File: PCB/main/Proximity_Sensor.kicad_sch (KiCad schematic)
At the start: 9 parts, among them U6 VL6180XV0NR_1

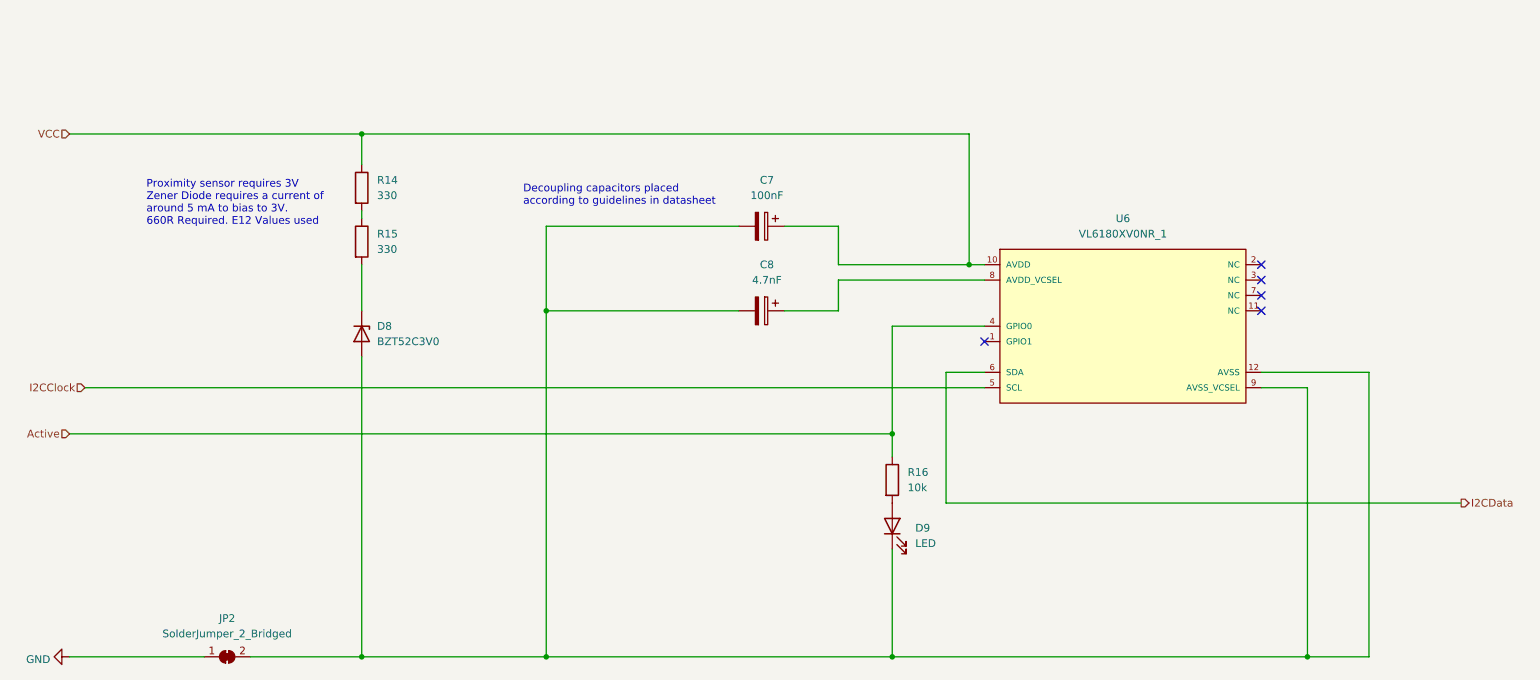
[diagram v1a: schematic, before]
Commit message: Add power flags
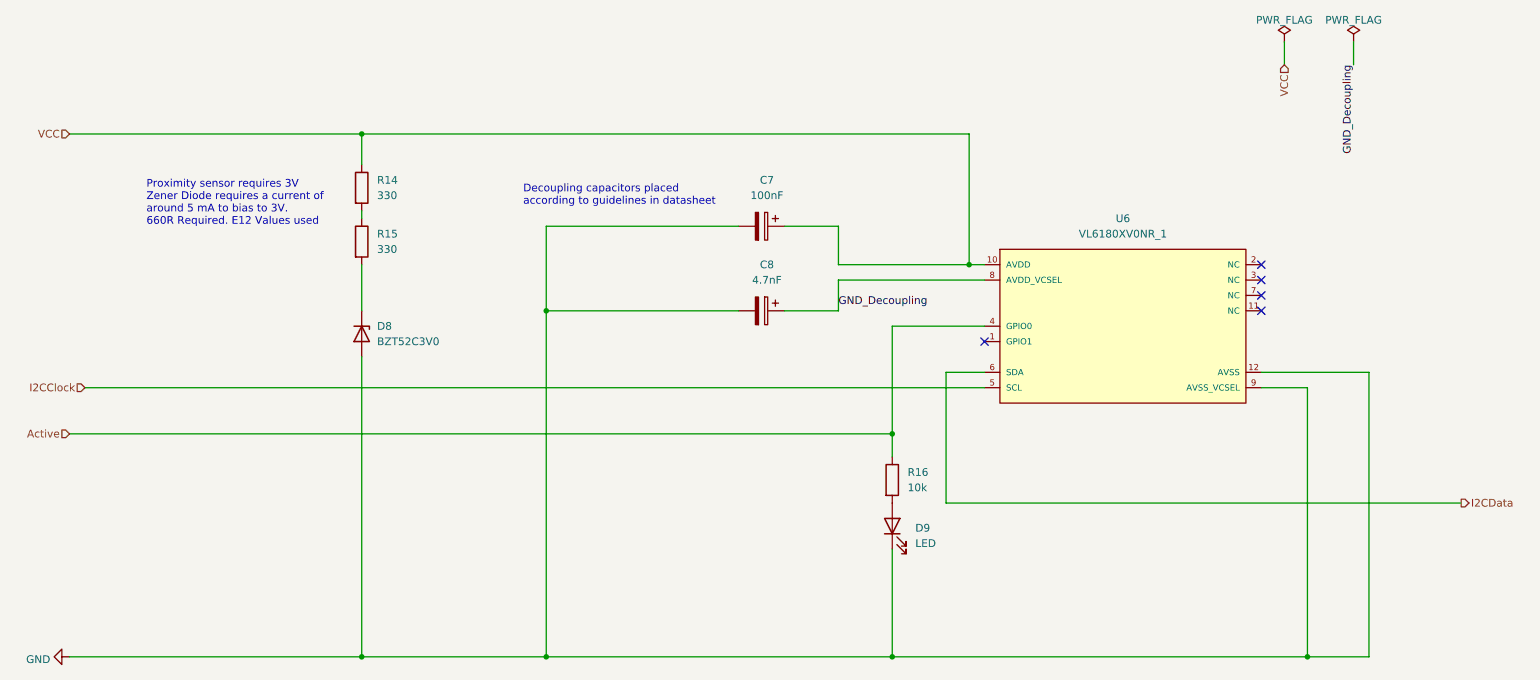
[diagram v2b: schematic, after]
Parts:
- removed JP2: SolderJumper_2_Bridged, Jumper:SolderJumper-2_P1.3mm_Bridged2Bar_Pad1.0x1.5mm, symbol Jumper:SolderJumper_2_Bridged
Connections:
- net GND: now also C7.2, C8.2, D8.2 (A), D9.1 (K), U6.12 (AVSS), U6.9 (AVSS_VCSEL)
- net GND_Decoupling: now reaches C8.1, U6.8 (AVDD_VCSEL)
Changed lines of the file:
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@@
+    (stroke (width 0) (type default) (color 0 0 0 0))
+  )
+  (wire (pts (xy 248.92 22.86) (xy 248.92 26.67))
     (stroke (width 0) (type default) (color 0 0 0 0))
   )
@@
     (stroke (width 0) (type default) (color 0 0 0 0))
   )
-  (wire (pts (xy 36.83 124.46) (xy 59.055 124.46))
-    (stroke (width 0) (type default) (color 0 0 0 0))
-  )
   (wire (pts (xy 163.83 59.69) (xy 163.83 53.34))
     (stroke (width 0) (type default) (color 0 0 0 0))
@@
     (stroke (width 0) (type default) (color 0 0 0 0))
   )
-  (wire (pts (xy 66.675 124.46) (xy 85.09 124.46))
+  (wire (pts (xy 36.83 124.46) (xy 85.09 124.46))
     (stroke (width 0) (type default) (color 0 0 0 0))
   )
@@
   )
   (wire (pts (xy 185.42 59.69) (xy 187.96 59.69))
+    (stroke (width 0) (type default) (color 0 0 0 0))
+  )
+  (wire (pts (xy 237.49 22.86) (xy 237.49 26.67))
     (stroke (width 0) (type default) (color 0 0 0 0))
   )
@@
     (effects (font (size 1.27 1.27)) (justify left bottom))
   )
+  (label "GND_Decoupling" (at 163.83 66.675 0)
+    (effects (font (size 1.27 1.27)) (justify left bottom))
+  )
+  (label "GND_Decoupling" (at 248.92 26.67 270)
+    (effects (font (size 1.27 1.27)) (justify right bottom))
+  )
   (hierarchical_label "Active" (shape input) (at 36.83 87.63 180)
     (effects (font (size 1.27 1.27)) (justify right))
   )
   (hierarchical_label "VCC" (shape input) (at 36.83 38.1 180)
+    (effects (font (size 1.27 1.27)) (justify right))
+  )
+  (hierarchical_label "VCC" (shape input) (at 237.49 26.67 270)
     (effects (font (size 1.27 1.27)) (justify right))
   )
@@
     (pin "2")
   )
-  (symbol (lib_id "Jumper:SolderJumper_2_Bridged") (at 62.865 124.46 0) (unit 1)
-    (in_bom yes) (on_board yes) (fields_autoplaced)
-    (property "Reference" "JP2" (id 0) (at 62.865 118.11 0))
-    (property "Value" "SolderJumper_2_Bridged" (id 1) (at 62.865 120.65 0))
-    (property "Footprint" "Jumper:SolderJumper-2_P1.3mm_Bridged2Bar_Pad1.0x1.5mm" (id 2) (at 62.865 124.46 0)
-      (effects (font (size 1.27 1.27)) hide)
-    )
-    (property "Datasheet" "~" (id 3) (at 62.865 124.46 0)
-      (effects (font (size 1.27 1.27)) hide)
-    )
-    (pin "1")
-    (pin "2")
+  (symbol (lib_id "power:PWR_FLAG") (at 237.49 22.86 0) (unit 1)
+    (in_bom yes) (on_board yes) (fields_autoplaced)
+    (property "Reference" "#FLG04" (id 0) (at 237.49 20.955 0)
+      (effects (font (size 1.27 1.27)) hide)
+    )
+    (property "Value" "PWR_FLAG" (id 1) (at 237.49 19.2842 0))
+    (property "Footprint" "" (id 2) (at 237.49 22.86 0)
+      (effects (font (size 1.27 1.27)) hide)
+    )
+    (property "Datasheet" "~" (id 3) (at 237.49 22.86 0)
+      (effects (font (size 1.27 1.27)) hide)
+    )
+    (pin "1")
   )
   (symbol (lib_id "power:GND") (at 36.83 124.46 270) (unit 1)
@@
     (pin "2")
   )
+  (symbol (lib_id "power:PWR_FLAG") (at 248.92 22.86 0) (unit 1)
+    (in_bom yes) (on_board yes) (fields_autoplaced)
+    (property "Reference" "#FLG05" (id 0) (at 248.92 20.955 0)
+      (effects (font (size 1.27 1.27)) hide)
+    )
+    (property "Value" "PWR_FLAG" (id 1) (at 248.92 19.2842 0))
+    (property "Footprint" "" (id 2) (at 248.92 22.86 0)
+      (effects (font (size 1.27 1.27)) hide)
+    )
+    (property "Datasheet" "~" (id 3) (at 248.92 22.86 0)
+      (effects (font (size 1.27 1.27)) hide)
+    )
+    (pin "1")
+  )
   (symbol (lib_id "EEE3088Components:VL6180XV0NR_1") (at 185.42 59.69 0) (unit 1)

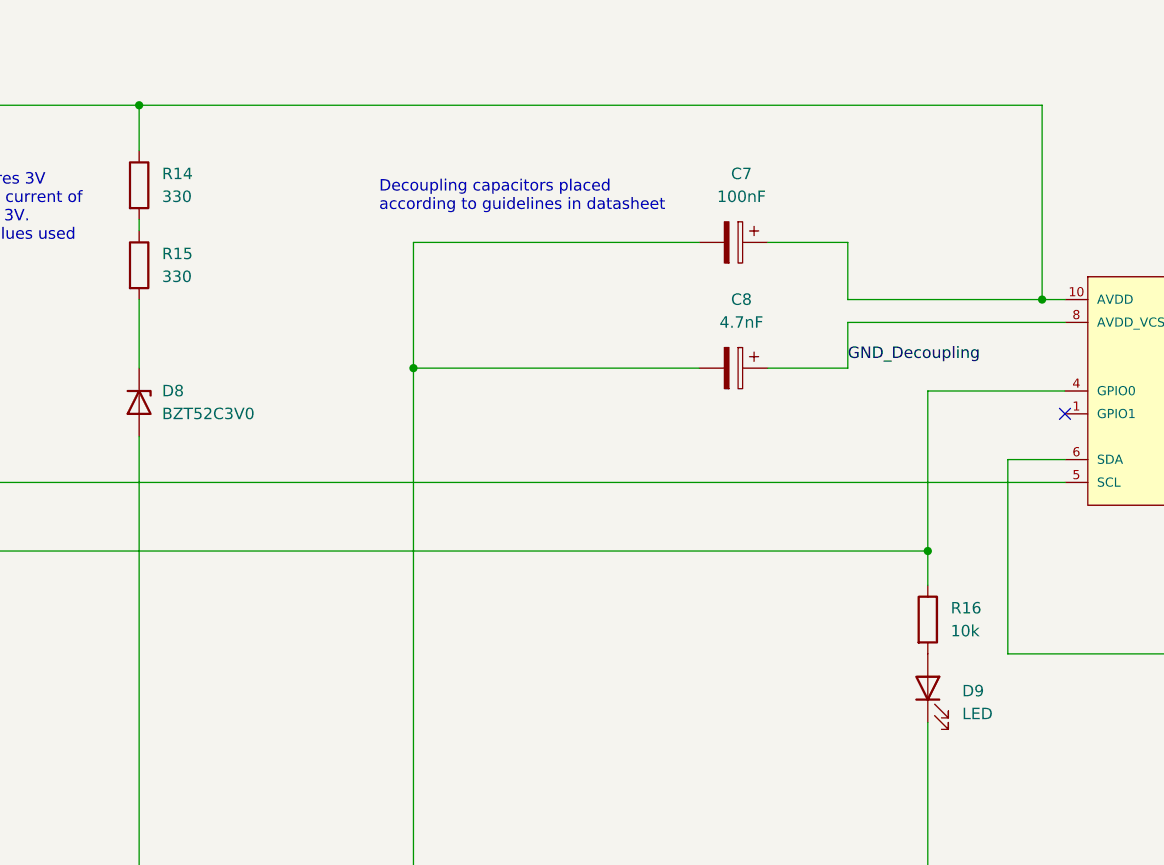
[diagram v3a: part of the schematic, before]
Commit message: Add footprints
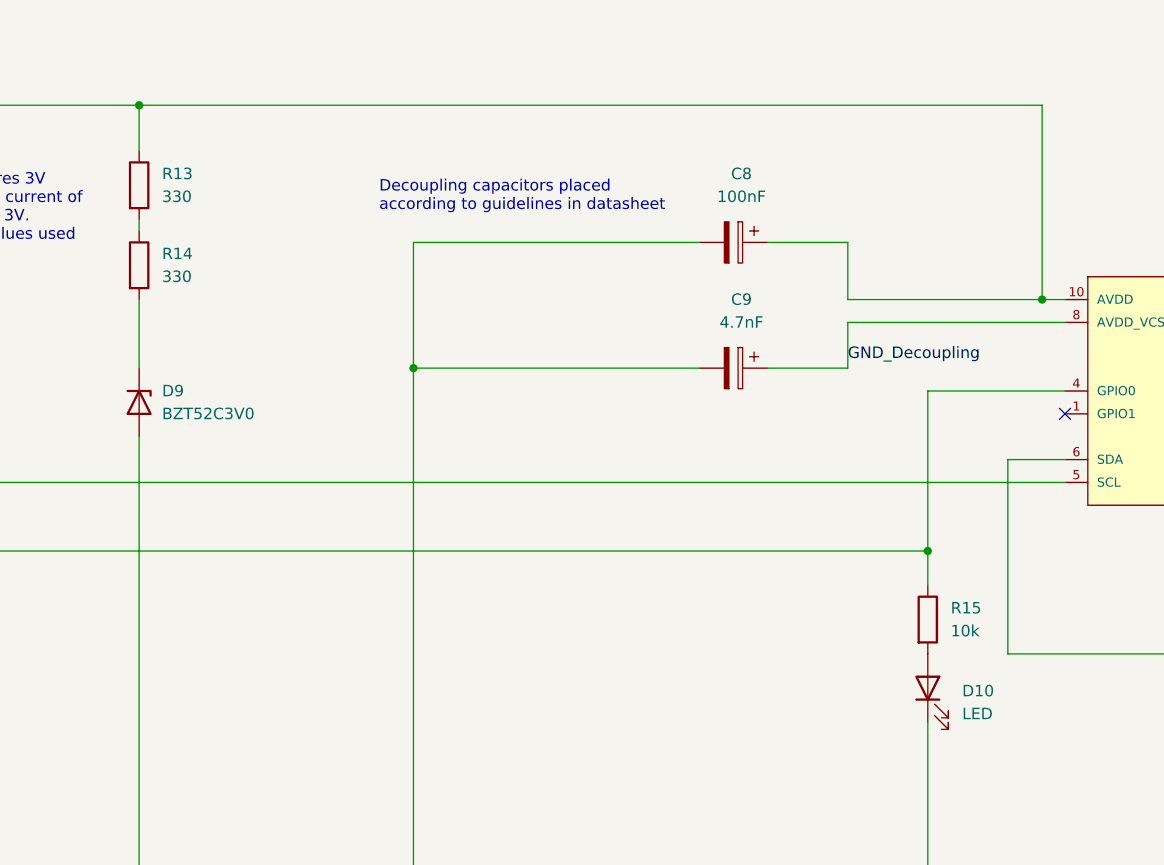
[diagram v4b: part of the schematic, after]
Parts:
- U6: footprint STMicroelectronics-VL6180XV0NR_1-* -> Footprint_EEE3088F:LGA-12_L4.8-W2.8-P0.75-BL; symbol EEE3088Components:VL6180XV0NR_1 -> Symbol_EEE3088F:VL6180XV0NR_1
- renumbered C7 to C8, C8 to C9, D9 to D10, D8 to D9, R14 to R13, R15 to R14, R16 to R15
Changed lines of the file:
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@@
   (symbol (lib_id "Device:R") (at 85.09 46.99 0) (unit 1)
     (in_bom yes) (on_board yes) (fields_autoplaced)
-    (property "Reference" "R14" (id 0) (at 87.63 45.7199 0)
+    (property "Reference" "R13" (id 0) (at 87.63 45.7199 0)
       (effects (font (size 1.27 1.27)) (justify left))
     )
@@
   (symbol (lib_id "Device:C_Polarized") (at 151.13 53.34 270) (unit 1)
     (in_bom yes) (on_board yes) (fields_autoplaced)
-    (property "Reference" "C7" (id 0) (at 152.019 45.72 90))
+    (property "Reference" "C8" (id 0) (at 152.019 45.72 90))
     (property "Value" "100nF" (id 1) (at 152.019 48.26 90))
     (property "Footprint" "Capacitor_SMD:C_0402_1005Metric" (id 2) (at 147.32 54.3052 0)
@@
   (symbol (lib_id "power:GND") (at 36.83 124.46 270) (unit 1)
     (in_bom yes) (on_board yes) (fields_autoplaced)
-    (property "Reference" "#PWR0103" (id 0) (at 30.48 124.46 0)
+    (property "Reference" "#PWR035" (id 0) (at 30.48 124.46 0)
       (effects (font (size 1.27 1.27)) hide)
     )
@@
   (symbol (lib_id "Device:R") (at 172.72 95.25 0) (unit 1)
     (in_bom yes) (on_board yes) (fields_autoplaced)
-    (property "Reference" "R16" (id 0) (at 175.26 93.9799 0)
+    (property "Reference" "R15" (id 0) (at 175.26 93.9799 0)
       (effects (font (size 1.27 1.27)) (justify left))
     )
@@
   (symbol (lib_id "Device:R") (at 85.09 55.88 0) (unit 1)
     (in_bom yes) (on_board yes) (fields_autoplaced)
-    (property "Reference" "R15" (id 0) (at 87.63 54.6099 0)
+    (property "Reference" "R14" (id 0) (at 87.63 54.6099 0)
       (effects (font (size 1.27 1.27)) (justify left))
     )
@@
   (symbol (lib_id "Device:C_Polarized") (at 151.13 67.31 270) (unit 1)
     (in_bom yes) (on_board yes) (fields_autoplaced)
-    (property "Reference" "C8" (id 0) (at 152.019 59.69 90))
+    (property "Reference" "C9" (id 0) (at 152.019 59.69 90))
     (property "Value" "4.7nF" (id 1) (at 152.019 62.23 90))
     (property "Footprint" "Capacitor_SMD:C_0402_1005Metric" (id 2) (at 147.32 68.2752 0)
@@
   (symbol (lib_id "Diode:BZT52Bxx") (at 85.09 71.12 270) (unit 1)
     (in_bom yes) (on_board yes) (fields_autoplaced)
-    (property "Reference" "D8" (id 0) (at 87.63 69.8499 90)
+    (property "Reference" "D9" (id 0) (at 87.63 69.8499 90)
       (effects (font (size 1.27 1.27)) (justify left))
     )
@@
   (symbol (lib_id "Device:LED") (at 172.72 102.87 90) (unit 1)
     (in_bom yes) (on_board yes) (fields_autoplaced)
-    (property "Reference" "D9" (id 0) (at 176.53 103.1874 90)
+    (property "Reference" "D10" (id 0) (at 176.53 103.1874 90)
       (effects (font (size 1.27 1.27)) (justify right))
     )
@@
     (pin "1")
   )
-  (symbol (lib_id "EEE3088Components:VL6180XV0NR_1") (at 185.42 59.69 0) (unit 1)
+  (symbol (lib_id "Symbol_EEE3088F:VL6180XV0NR_1") (at 185.42 59.69 0) (unit 1)
     (in_bom yes) (on_board yes) (fields_autoplaced)
     (property "Reference" "U6" (id 0) (at 210.82 52.07 0))
     (property "Value" "VL6180XV0NR_1" (id 1) (at 210.82 54.61 0))
-    (property "Footprint" "STMicroelectronics-VL6180XV0NR_1-*" (id 2) (at 185.42 49.53 0)
+    (property "Footprint" "Footprint_EEE3088F:LGA-12_L4.8-W2.8-P0.75-BL" (id 2) (at 185.42 49.53 0)
       (effects (font (size 1.27 1.27)) (justify left) hide)
     )

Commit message: Small changes
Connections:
- net GND_Decoupling is gone; now on net VCC: C9.1, U6.8 (AVDD_VCSEL)
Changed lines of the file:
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@@
   (junction (at 172.72 87.63) (diameter 0) (color 0 0 0 0)
   )
+  (junction (at 172.72 38.1) (diameter 0) (color 0 0 0 0)
+  )
   (junction (at 85.09 38.1) (diameter 0) (color 0 0 0 0)
   )
@@
   )
   (junction (at 172.72 124.46) (diameter 0) (color 0 0 0 0)
+  )
+  (junction (at 172.72 62.23) (diameter 0) (color 0 0 0 0)
   )
   (junction (at 85.09 124.46) (diameter 0) (color 0 0 0 0)
@@
     (stroke (width 0) (type default) (color 0 0 0 0))
   )
+  (wire (pts (xy 172.72 38.1) (xy 185.42 38.1))
+    (stroke (width 0) (type default) (color 0 0 0 0))
+  )
   (wire (pts (xy 115.57 124.46) (xy 172.72 124.46))
     (stroke (width 0) (type default) (color 0 0 0 0))
@@
     (stroke (width 0) (type default) (color 0 0 0 0))
   )
+  (wire (pts (xy 172.72 62.23) (xy 163.83 62.23))
+    (stroke (width 0) (type default) (color 0 0 0 0))
+  )
   (wire (pts (xy 163.83 62.23) (xy 163.83 67.31))
     (stroke (width 0) (type default) (color 0 0 0 0))
@@
     (stroke (width 0) (type default) (color 0 0 0 0))
   )
-  (wire (pts (xy 248.92 22.86) (xy 248.92 26.67))
-    (stroke (width 0) (type default) (color 0 0 0 0))
-  )
   (wire (pts (xy 154.94 53.34) (xy 163.83 53.34))
     (stroke (width 0) (type default) (color 0 0 0 0))
   )
-  (wire (pts (xy 85.09 38.1) (xy 185.42 38.1))
+  (wire (pts (xy 85.09 38.1) (xy 172.72 38.1))
     (stroke (width 0) (type default) (color 0 0 0 0))
   )
@@
     (stroke (width 0) (type default) (color 0 0 0 0))
   )
+  (wire (pts (xy 172.72 38.1) (xy 172.72 62.23))
+    (stroke (width 0) (type default) (color 0 0 0 0))
+  )
   (wire (pts (xy 185.42 38.1) (xy 185.42 59.69))
     (stroke (width 0) (type default) (color 0 0 0 0))
@@
     (stroke (width 0) (type default) (color 0 0 0 0))
   )
-  (wire (pts (xy 187.96 62.23) (xy 163.83 62.23))
+  (wire (pts (xy 187.96 62.23) (xy 172.72 62.23))
     (stroke (width 0) (type default) (color 0 0 0 0))
   )
@@
     (effects (font (size 1.27 1.27)) (justify left bottom))
   )
-  (label "GND_Decoupling" (at 163.83 66.675 0)
-    (effects (font (size 1.27 1.27)) (justify left bottom))
-  )
-  (label "GND_Decoupling" (at 248.92 26.67 270)
-    (effects (font (size 1.27 1.27)) (justify right bottom))
-  )
   (hierarchical_label "Active" (shape input) (at 36.83 87.63 180)
     (effects (font (size 1.27 1.27)) (justify right))
@@
     (pin "2")
   )
-  (symbol (lib_id "power:PWR_FLAG") (at 248.92 22.86 0) (unit 1)
-    (in_bom yes) (on_board yes) (fields_autoplaced)
-    (property "Reference" "#FLG05" (id 0) (at 248.92 20.955 0)
-      (effects (font (size 1.27 1.27)) hide)
-    )
-    (property "Value" "PWR_FLAG" (id 1) (at 248.92 19.2842 0))
-    (property "Footprint" "" (id 2) (at 248.92 22.86 0)
-      (effects (font (size 1.27 1.27)) hide)
-    )
-    (property "Datasheet" "~" (id 3) (at 248.92 22.86 0)
-      (effects (font (size 1.27 1.27)) hide)
-    )
-    (pin "1")
-  )
   (symbol (lib_id "Symbol_EEE3088F:VL6180XV0NR_1") (at 185.42 59.69 0) (unit 1)

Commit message: Updated BOM
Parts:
- C8: JLC Part # (none) -> C307331; Price (none) -> 0.0065
- C9: JLC Part # (none) -> C1538; Price (none) -> 0.0011
- D10: JLC Part # (none) -> C2286; Price (none) -> 0.0032
- D9: JLC Part # (none) -> C266562; Price (none) -> 0.0136
- R13, R14: JLC Part # (none) -> C25104; Price (none) -> 0.0007
- R15: JLC Part # (none) -> C25744; Price (none) -> 0.0007
- U6: JLC Part # (none) -> C2655167; Price (none) -> 1.9575
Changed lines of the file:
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@@
+      (effects (font (size 1.27 1.27)) hide)
+    )
+    (property "JLC Part #" " C25104" (id 5) (at 85.09 46.99 0)
+      (effects (font (size 1.27 1.27)) hide)
+    )
+    (property "Price" "0.0007" (id 6) (at 85.09 46.99 0)
       (effects (font (size 1.27 1.27)) hide)
     )
@@
       (effects (font (size 1.27 1.27)) hide)
     )
+    (property "JLC Part #" " C307331" (id 5) (at 151.13 53.34 0)
+      (effects (font (size 1.27 1.27)) hide)
+    )
+    (property "Price" "0.0065" (id 6) (at 151.13 53.34 0)
+      (effects (font (size 1.27 1.27)) hide)
+    )
     (pin "1")
     (pin "2")
@@
       (effects (font (size 1.27 1.27)) hide)
     )
+    (property "JLC Part #" " C25744 " (id 6) (at 172.72 95.25 0)
+      (effects (font (size 1.27 1.27)) hide)
+    )
+    (property "Price" "0.0007" (id 7) (at 172.72 95.25 0)
+      (effects (font (size 1.27 1.27)) hide)
+    )
     (pin "1")
     (pin "2")
@@
     )
     (property "JLCPart" " C25104" (id 4) (at 85.09 55.88 0)
+      (effects (font (size 1.27 1.27)) hide)
+    )
+    (property "JLC Part #" " C25104" (id 5) (at 85.09 55.88 0)
+      (effects (font (size 1.27 1.27)) hide)
+    )
+    (property "Price" "0.0007" (id 6) (at 85.09 55.88 0)
       (effects (font (size 1.27 1.27)) hide)
     )
@@
       (effects (font (size 1.27 1.27)) hide)
     )
+    (property "JLC Part #" " C1538" (id 5) (at 151.13 67.31 0)
+      (effects (font (size 1.27 1.27)) hide)
+    )
+    (property "Price" "0.0011" (id 6) (at 151.13 67.31 0)
+      (effects (font (size 1.27 1.27)) hide)
+    )
     (pin "1")
     (pin "2")
@@
     )
     (property "JLCPartNumber" " C266562" (id 4) (at 85.09 71.12 90)
+      (effects (font (size 1.27 1.27)) hide)
+    )
+    (property "JLC Part #" " C266562" (id 5) (at 85.09 71.12 0)
+      (effects (font (size 1.27 1.27)) hide)
+    )
+    (property "Price" "0.0136" (id 6) (at 85.09 71.12 0)
       (effects (font (size 1.27 1.27)) hide)
     )
@@
     )
     (property "JLCPart" "C2286" (id 4) (at 172.72 102.87 90)
+      (effects (font (size 1.27 1.27)) hide)
+    )
+    (property "JLC Part #" "C2286" (id 5) (at 172.72 102.87 0)
+      (effects (font (size 1.27 1.27)) hide)
+    )
+    (property "Price" "0.0032" (id 6) (at 172.72 102.87 0)
       (effects (font (size 1.27 1.27)) hide)
     )
@@
       (effects (font (size 1.27 1.27)) hide)
     )
+    (property "JLC Part #" " C2655167" (id 28) (at 185.42 59.69 0)
+      (effects (font (size 1.27 1.27)) hide)
+    )
+    (property "Price" "1.9575" (id 29) (at 185.42 59.69 0)
+      (effects (font (size 1.27 1.27)) hide)
+    )

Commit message: Updated BOM
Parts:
- R15: JLC Part # C25744 -> C25744
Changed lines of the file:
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@@
       (effects (font (size 1.27 1.27)) hide)
     )
-    (property "JLC Part #" " C25744 " (id 6) (at 172.72 95.25 0)
+    (property "JLC Part #" "C25744" (id 6) (at 172.72 95.25 0)
       (effects (font (size 1.27 1.27)) hide)
     )
